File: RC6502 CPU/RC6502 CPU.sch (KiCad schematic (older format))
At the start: 10 parts, among them J1 CONN_01X39, J2 IRQ OnBus, J3 NMI OnBus, U1 WD65C02, U2 74HCT04

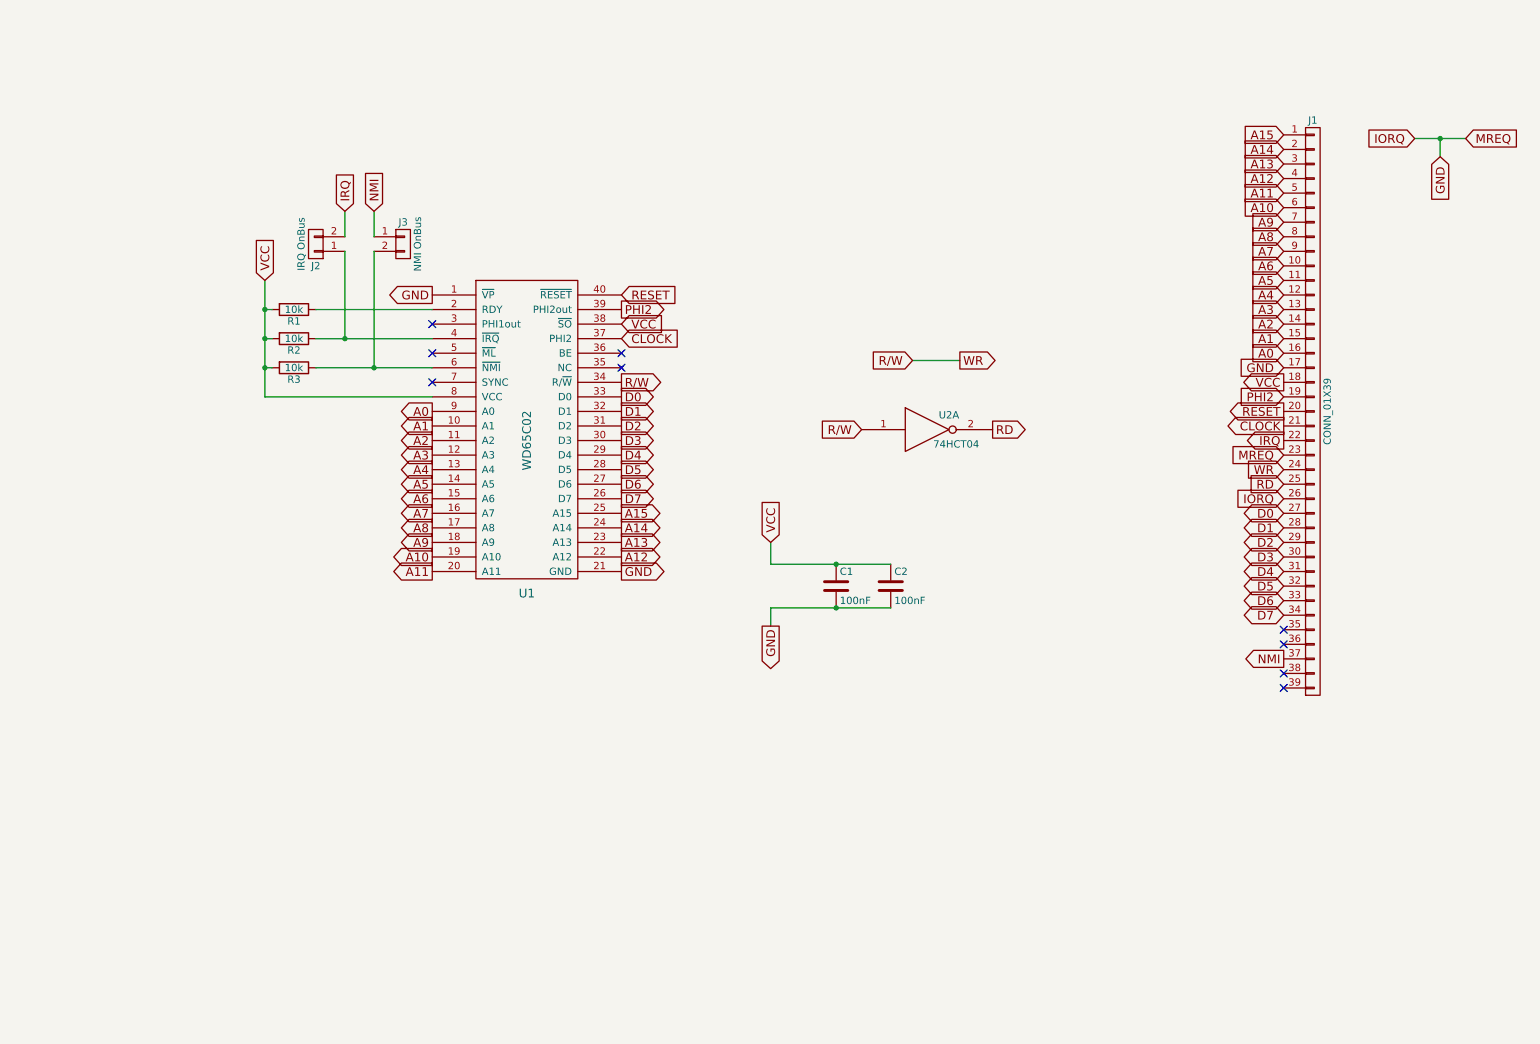
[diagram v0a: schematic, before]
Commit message: Added oscillator to CPU board
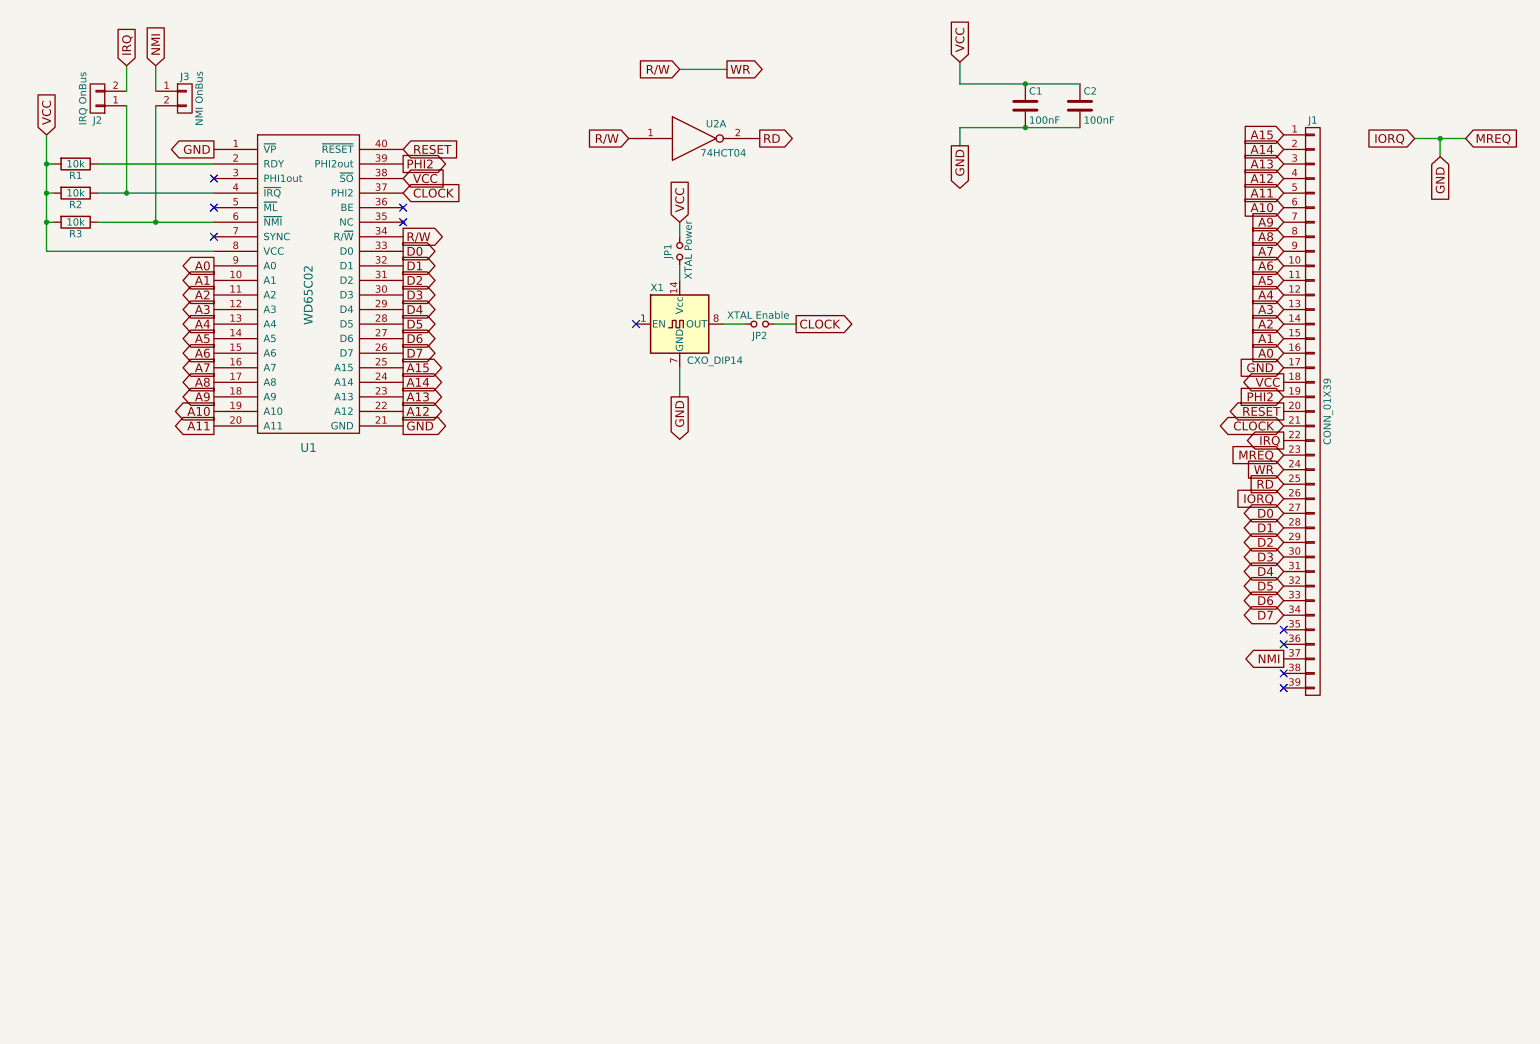
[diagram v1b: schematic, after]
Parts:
- added JP1: XTAL Power, Pin_Headers:Pin_Header_Angled_1x02_Pitch2.54mm, symbol Jumper_NO_Small
- added JP2: XTAL Enable, Pin_Headers:Pin_Header_Angled_1x02_Pitch2.54mm, symbol Jumper_NO_Small
- added X1: CXO_DIP14, Oscillators:Oscillator_DIP-14, symbol CXO_DIP14
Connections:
- net CLOCK: now also JP2.1
- net GND: now also X1.7 (GND)
- net VCC: now also JP1.2
- new net: JP1.1, X1.14 (Vcc)
- new net: JP2.2, X1.8 (OUT)
- no-connect marks 9 -> 10
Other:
- moved on the sheet: C1, C2, J2, J3, R1, R2, R3, U1, U2A

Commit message: Pullups changed to 3.3K and added VP jumper
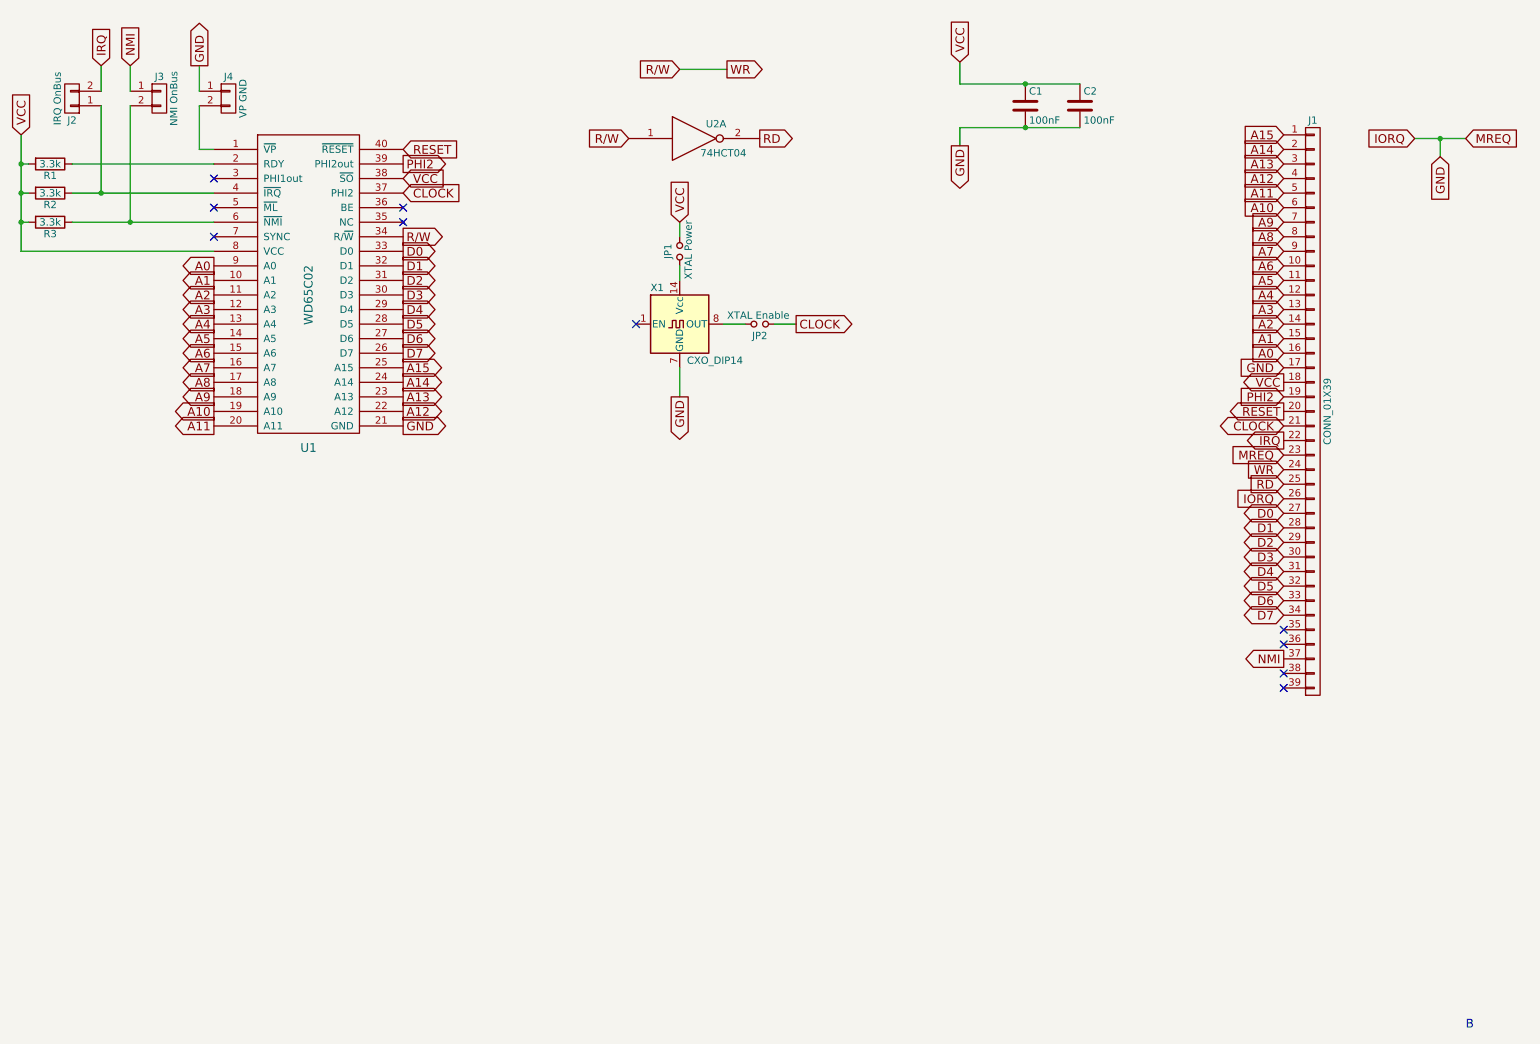
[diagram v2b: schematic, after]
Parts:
- added J4: VP GND, Pin_Headers:Pin_Header_Angled_1x02_Pitch2.54mm, symbol CONN_01X02
- R1, R2, R3: value 10k -> 3.3k
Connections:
- net GND: now also J4.1 (P1); no longer U1.1 (~VP)
- new net: J4.2 (P2), U1.1 (~VP)
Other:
- note added: "B"
- moved on the sheet: J2, J3, R1, R2, R3
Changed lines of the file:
@@
 L R R1
 U 1 1 590BA496
-P 1050 1700
-F 0 "R1" V 1130 1700 50  0000 C CNN
-F 1 "10k" V 1050 1700 50  0000 C CNN
-F 2 "Resistors_THT:R_Axial_DIN0207_L6.3mm_D2.5mm_P10.16mm_Horizontal" V 980 1700 50  0001 C CNN
-F 3 "" H 1050 1700 50  0001 C CNN
-	1    1050 1700
+P 875 1700
+F 0 "R1" V 955 1700 50  0000 C CNN
+F 1 "3.3k" V 875 1700 50  0000 C CNN
+F 2 "Resistors_THT:R_Axial_DIN0207_L6.3mm_D2.5mm_P10.16mm_Horizontal" V 805 1700 50  0001 C CNN
+F 3 "" H 875 1700 50  0001 C CNN
+	1    875  1700
 	0    1    1    0
 $EndComp
@@
 L R R2
 U 1 1 590BA57A
-P 1050 1900
-F 0 "R2" V 1130 1900 50  0000 C CNN
-F 1 "10k" V 1050 1900 50  0000 C CNN
-F 2 "Resistors_THT:R_Axial_DIN0207_L6.3mm_D2.5mm_P10.16mm_Horizontal" V 980 1900 50  0001 C CNN
-F 3 "" H 1050 1900 50  0001 C CNN
-	1    1050 1900
+P 875 1900
+F 0 "R2" V 955 1900 50  0000 C CNN
+F 1 "3.3k" V 875 1900 50  0000 C CNN
+F 2 "Resistors_THT:R_Axial_DIN0207_L6.3mm_D2.5mm_P10.16mm_Horizontal" V 805 1900 50  0001 C CNN
+F 3 "" H 875 1900 50  0001 C CNN
+	1    875  1900
 	0    1    1    0
 $EndComp
@@
 L R R3
 U 1 1 590BA5A2
-P 1050 2100
-F 0 "R3" V 1130 2100 50  0000 C CNN
-F 1 "10k" V 1050 2100 50  0000 C CNN
-F 2 "Resistors_THT:R_Axial_DIN0207_L6.3mm_D2.5mm_P10.16mm_Horizontal" V 980 2100 50  0001 C CNN
-F 3 "" H 1050 2100 50  0001 C CNN
-	1    1050 2100
+P 875 2100
+F 0 "R3" V 955 2100 50  0000 C CNN
+F 1 "3.3k" V 875 2100 50  0000 C CNN
+F 2 "Resistors_THT:R_Axial_DIN0207_L6.3mm_D2.5mm_P10.16mm_Horizontal" V 805 2100 50  0001 C CNN
+F 3 "" H 875 2100 50  0001 C CNN
+	1    875  2100
 	0    1    1    0
 $EndComp
@@
 	1    0    0    -1
 $EndComp
-Text GLabel 850  1500 1    60   Input ~ 0
+Text GLabel 675  1500 1    60   Input ~ 0
 VCC
 $Comp
@@
 IORQ
 Wire Wire Line
-	850  1500 850  2300
-Wire Wire Line
-	850  2300 2000 2300
-Wire Wire Line
-	900  2100 850  2100
-Connection ~ 850  2100
-Wire Wire Line
-	900  1900 850  1900
-Connection ~ 850  1900
-Wire Wire Line
-	900  1700 850  1700
-Connection ~ 850  1700
-Wire Wire Line
-	1200 1700 2000 1700
-Wire Wire Line
-	1200 1900 2000 1900
-Wire Wire Line
-	1200 2100 2000 2100
+	675  1500 675  2300
+Wire Wire Line
+	675  2300 2000 2300
+Wire Wire Line
+	725  2100 675  2100
+Connection ~ 675  2100
+Wire Wire Line
+	725  1900 675  1900
+Connection ~ 675  1900
+Wire Wire Line
+	725  1700 675  1700
+Connection ~ 675  1700
+Wire Wire Line
+	1025 1700 2000 1700
+Wire Wire Line
+	1025 1900 2000 1900
+Wire Wire Line
+	1025 2100 2000 2100
 Wire Wire Line
 	10250 1525 10600 1525
@@
 Text GLabel 9350 3500 0    60   BiDi ~ 0
 CLOCK
-Text GLabel 2000 1600 0    60   Output ~ 0
+Text GLabel 1900 1025 1    60   Output ~ 0
 GND
 Text GLabel 9350 3600 0    60   Output ~ 0
 IRQ
-Text GLabel 1400 1025 1    60   Input ~ 0
+Text GLabel 1225 1025 1    60   Input ~ 0
 IRQ
 Wire Wire Line
-	1400 1300 1400 1900
-Connection ~ 1400 1900
-Text GLabel 1600 1025 1    60   Input ~ 0
+	1225 1300 1225 1900
+Connection ~ 1225 1900
+Text GLabel 1425 1025 1    60   Input ~ 0
 NMI
 Wire Wire Line
-	1600 1300 1600 2100
-Connection ~ 1600 2100
+	1425 1300 1425 2100
+Connection ~ 1425 2100
 Text GLabel 9350 4100 0    60   BiDi ~ 0
 D0
@@
 L CONN_01X02 J2
 U 1 1 590D2BF8
-P 1200 1250
-F 0 "J2" H 1200 1400 50  0000 C CNN
-F 1 "IRQ OnBus" V 1300 1250 50  0000 C CNN
-F 2 "Pin_Headers:Pin_Header_Angled_1x02_Pitch2.54mm" H 1200 1250 50  0001 C CNN
-F 3 "" H 1200 1250 50  0001 C CNN
-	1    1200 1250
+P 1025 1250
+F 0 "J2" H 1025 1400 50  0000 C CNN
+F 1 "IRQ OnBus" V 1125 1250 50  0000 C CNN
+F 2 "Pin_Headers:Pin_Header_Angled_1x02_Pitch2.54mm" H 1025 1250 50  0001 C CNN
+F 3 "" H 1025 1250 50  0001 C CNN
+	1    1025 1250
 	-1   0    0    1
 $EndComp
@@
 L CONN_01X02 J3
 U 1 1 590D2C70
-P 1800 1250
-F 0 "J3" H 1800 1400 50  0000 C CNN
-F 1 "NMI OnBus" V 1900 1250 50  0000 C CNN
-F 2 "Pin_Headers:Pin_Header_Angled_1x02_Pitch2.54mm" H 1800 1250 50  0001 C CNN
-F 3 "" H 1800 1250 50  0001 C CNN
-	1    1800 1250
-	1    0    0    -1
-$EndComp
-Wire Wire Line
-	1400 1025 1400 1200
-Wire Wire Line
-	1600 1025 1600 1200
+P 1625 1250
+F 0 "J3" H 1625 1400 50  0000 C CNN
+F 1 "NMI OnBus" V 1725 1250 50  0000 C CNN
+F 2 "Pin_Headers:Pin_Header_Angled_1x02_Pitch2.54mm" H 1625 1250 50  0001 C CNN
+F 3 "" H 1625 1250 50  0001 C CNN
+	1    1625 1250
+	1    0    0    -1
+$EndComp
+Wire Wire Line
+	1225 1025 1225 1200
+Wire Wire Line
+	1425 1025 1425 1200
 $Comp
 L C C1
@@
 Wire Wire Line
 	5850 2800 6000 2800
+$Comp
+L CONN_01X02 J4
+U 1 1 59304984
+P 2100 1250
+F 0 "J4" H 2100 1400 50  0000 C CNN
+F 1 "VP GND" V 2200 1250 50  0000 C CNN
+F 2 "Pin_Headers:Pin_Header_Angled_1x02_Pitch2.54mm" H 2100 1250 50  0001 C CNN
+F 3 "" H 2100 1250 50  0001 C CNN
+	1    2100 1250
+	1    0    0    -1
+$EndComp
+Wire Wire Line
+	1900 1600 1900 1300
+Wire Wire Line
+	1900 1200 1900 1025
+Wire Wire Line
+	1900 1600 2000 1600
+Text Notes 10600 7650 0    60   ~ 0
+B
 $EndSCHEMATC

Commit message: Put RDY and Sync on the bus
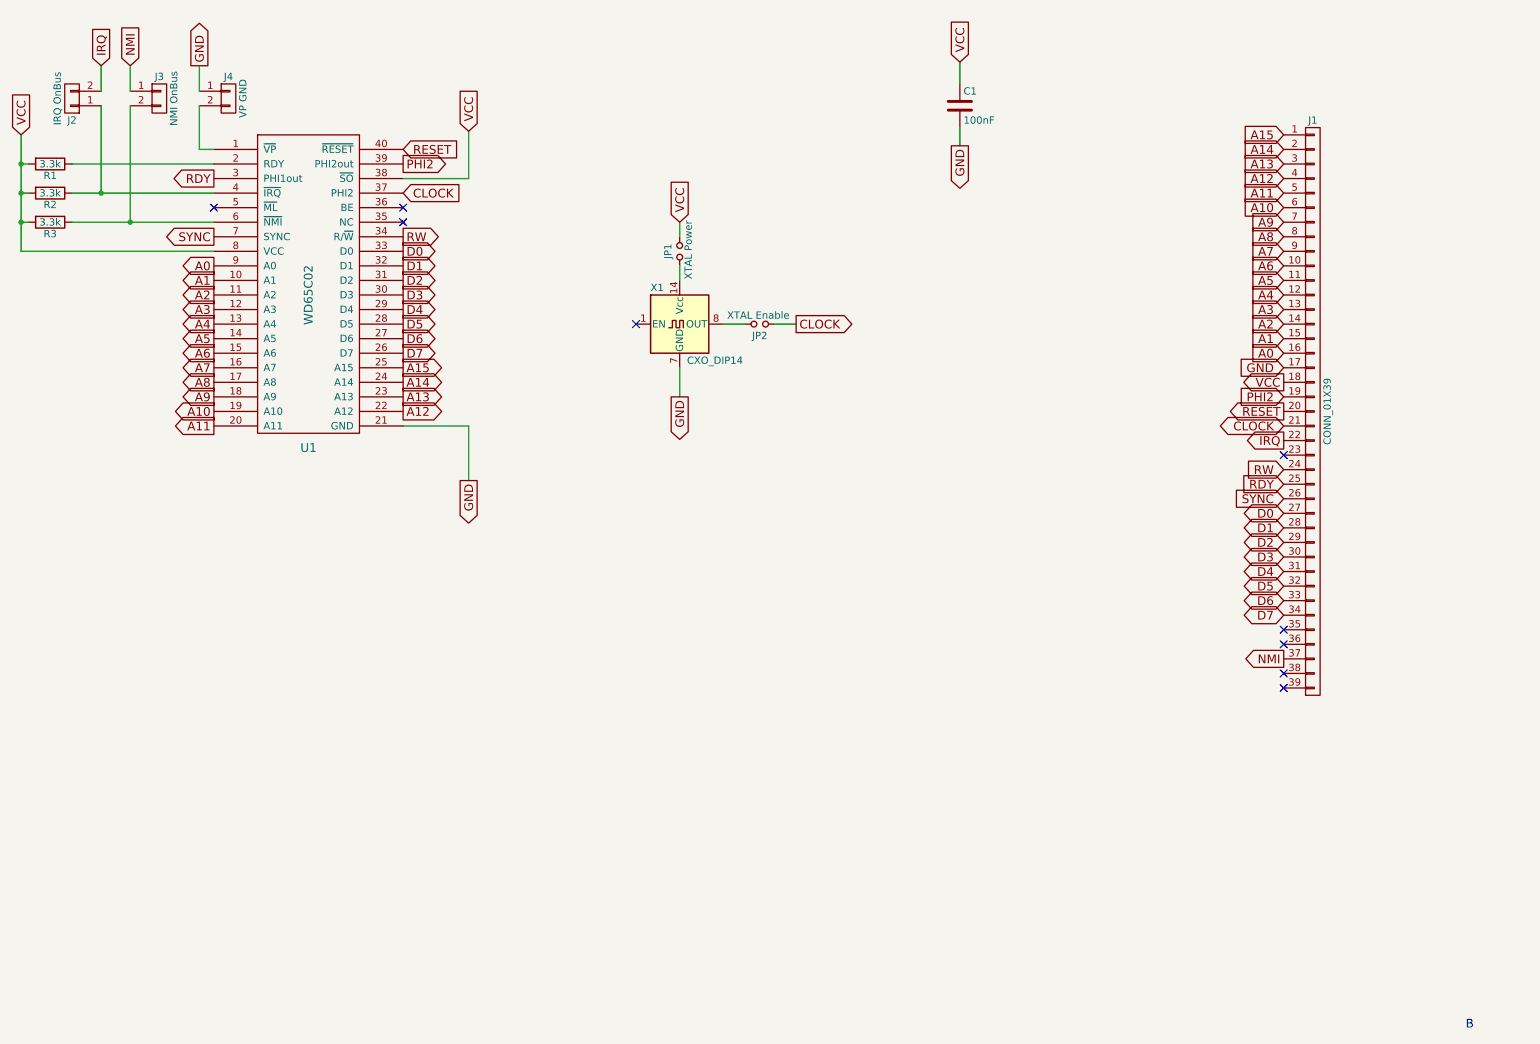
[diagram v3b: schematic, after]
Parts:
- removed C2: 100nF, Capacitors_THT:C_Disc_D4.7mm_W2.5mm_P5.00mm, symbol C
- removed U2: 74HCT04, Housings_DIP:DIP-14_W7.62mm_Socket, symbol 74HCT04
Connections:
- net RD is gone; now on net RDY: J1.25 (P25)
- net GND: no longer J1.23 (P23), J1.26 (P26)
- net RDY: now reaches U1.3 (PHI1out)
- net SYNC: now reaches U1.7 (SYNC)
- net SYNC: now also J1.26 (P26)
- net R/W renamed RW
- no-connect marks 10 -> 9
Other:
- moved on the sheet: C1
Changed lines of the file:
@@
 	1    0    0    -1
 $EndComp
-Text GLabel 3300 1800 2    60   Input ~ 0
+Text GLabel 3750 1475 1    60   Input ~ 0
 VCC
-Text GLabel 3300 3500 2    60   Output ~ 0
+Text GLabel 3750 3875 3    60   Output ~ 0
 GND
 Text GLabel 9350 3800 0    60   Input ~ 0
-WR
+RW
 Text GLabel 3300 2200 2    60   Output ~ 0
-R/W
-Text GLabel 9350 3900 0    60   Input ~ 0
-RD
-Text GLabel 9350 3700 0    60   Input ~ 0
-MREQ
-Text GLabel 9350 4000 0    60   Input ~ 0
-IORQ
-Text GLabel 10425 1650 3    60   Input ~ 0
-GND
-Text GLabel 10600 1525 2    60   Input ~ 0
-MREQ
-Text GLabel 10250 1525 0    60   Input ~ 0
-IORQ
+RW
 Wire Wire Line
 	675  1500 675  2300
@@
 Wire Wire Line
 	1025 2100 2000 2100
-Wire Wire Line
-	10250 1525 10600 1525
-Wire Wire Line
-	10425 1525 10425 1650
-Connection ~ 10425 1525
-Text GLabel 5200 1050 0    60   Input ~ 0
-R/W
-Text GLabel 5525 1050 2    60   Output ~ 0
-WR
-Wire Wire Line
-	5200 1050 5525 1050
-$Comp
-L 74HCT04 U2
-U 1 1 590BCEA0
-P 5300 1525
-F 0 "U2" H 5450 1625 50  0000 C CNN
-F 1 "74HCT04" H 5500 1425 50  0000 C CNN
-F 2 "Housings_DIP:DIP-14_W7.62mm_Socket" H 5300 1525 50  0001 C CNN
-F 3 "" H 5300 1525 50  0001 C CNN
-	1    5300 1525
-	1    0    0    -1
-$EndComp
-Text GLabel 4850 1525 0    60   Input ~ 0
-R/W
-Text GLabel 5750 1525 2    60   Output ~ 0
-RD
 Text GLabel 2000 2400 0    60   Output ~ 0
 A0
@@
 NoConn ~ 3300 2000
 NoConn ~ 2000 2000
-NoConn ~ 2000 1800
-NoConn ~ 2000 2200
 Text GLabel 3300 1900 2    60   Input ~ 0
 CLOCK
@@
 L C C1
 U 1 1 590DA9CE
-P 7575 1300
-F 0 "C1" H 7600 1400 50  0000 L CNN
-F 1 "100nF" H 7600 1200 50  0000 L CNN
-F 2 "Capacitors_THT:C_Disc_D4.7mm_W2.5mm_P5.00mm" H 7613 1150 50  0001 C CNN
-F 3 "" H 7575 1300 50  0001 C CNN
-	1    7575 1300
-	1    0    0    -1
-$EndComp
-Wire Wire Line
-	7125 1150 7950 1150
-Wire Wire Line
-	7125 1450 7950 1450
+P 7125 1300
+F 0 "C1" H 7150 1400 50  0000 L CNN
+F 1 "100nF" H 7150 1200 50  0000 L CNN
+F 2 "Capacitors_THT:C_Disc_D4.7mm_W2.5mm_P5.00mm" H 7163 1150 50  0001 C CNN
+F 3 "" H 7125 1300 50  0001 C CNN
+	1    7125 1300
+	1    0    0    -1
+$EndComp
 Text GLabel 7125 1575 3    60   Output ~ 0
 GND
@@
 Wire Wire Line
 	7125 1450 7125 1575
-$Comp
-L C C2
-U 1 1 590DB42B
-P 7950 1300
-F 0 "C2" H 7975 1400 50  0000 L CNN
-F 1 "100nF" H 7975 1200 50  0000 L CNN
-F 2 "Capacitors_THT:C_Disc_D4.7mm_W2.5mm_P5.00mm" H 7988 1150 50  0001 C CNN
-F 3 "" H 7950 1300 50  0001 C CNN
-	1    7950 1300
-	1    0    0    -1
-$EndComp
-Connection ~ 7575 1150
-Connection ~ 7575 1450
 $Comp
 L CXO_DIP14 X1
@@
 Text Notes 10600 7650 0    60   ~ 0
 B
+Wire Wire Line
+	3750 1475 3750 1800
+Wire Wire Line
+	3750 1800 3300 1800
+Wire Wire Line
+	3750 3500 3750 3875
+Wire Wire Line
+	3750 3500 3300 3500
+NoConn ~ 9350 3700
+Text GLabel 9350 3900 0    60   Input ~ 0
+RDY
+Text GLabel 9350 4000 0    60   Input ~ 0
+SYNC
+Text GLabel 2000 1800 0    60   Output ~ 0
+RDY
+Text GLabel 2000 2200 0    60   Output ~ 0
+SYNC
 $EndSCHEMATC
